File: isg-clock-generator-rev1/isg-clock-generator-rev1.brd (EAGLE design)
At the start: 76.2 x 76.2 mm, 154 parts, among them IC1 LMK03318RHSR, IC4 TPS7A8001DRBR, IC5 TPS7A8001DRBR, Q1 7M50072001, X1 OUT0_P, X2 OUT0_N, X3 OUT2_P, X4 PRIREF_P, X5 PRIREF_N, X6 V_INPUT

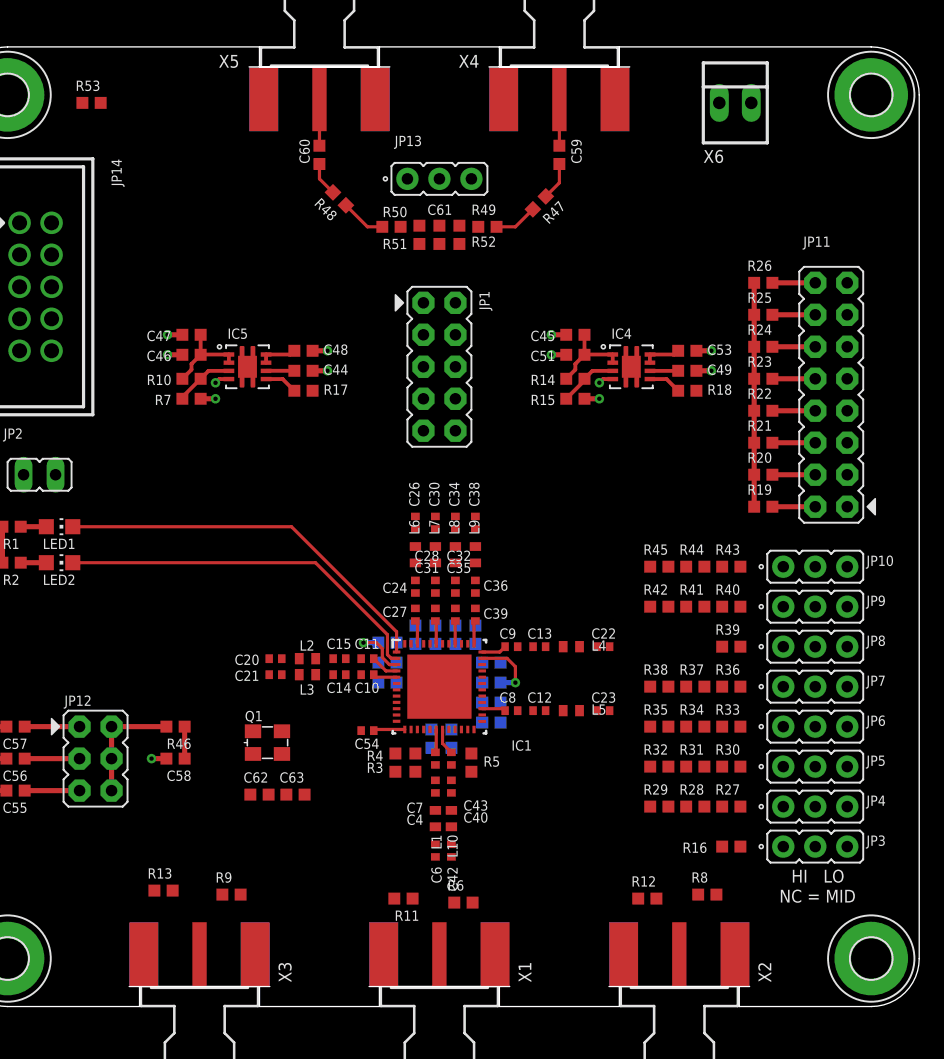
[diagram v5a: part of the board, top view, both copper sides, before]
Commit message: First-pass routing of high speed output signals
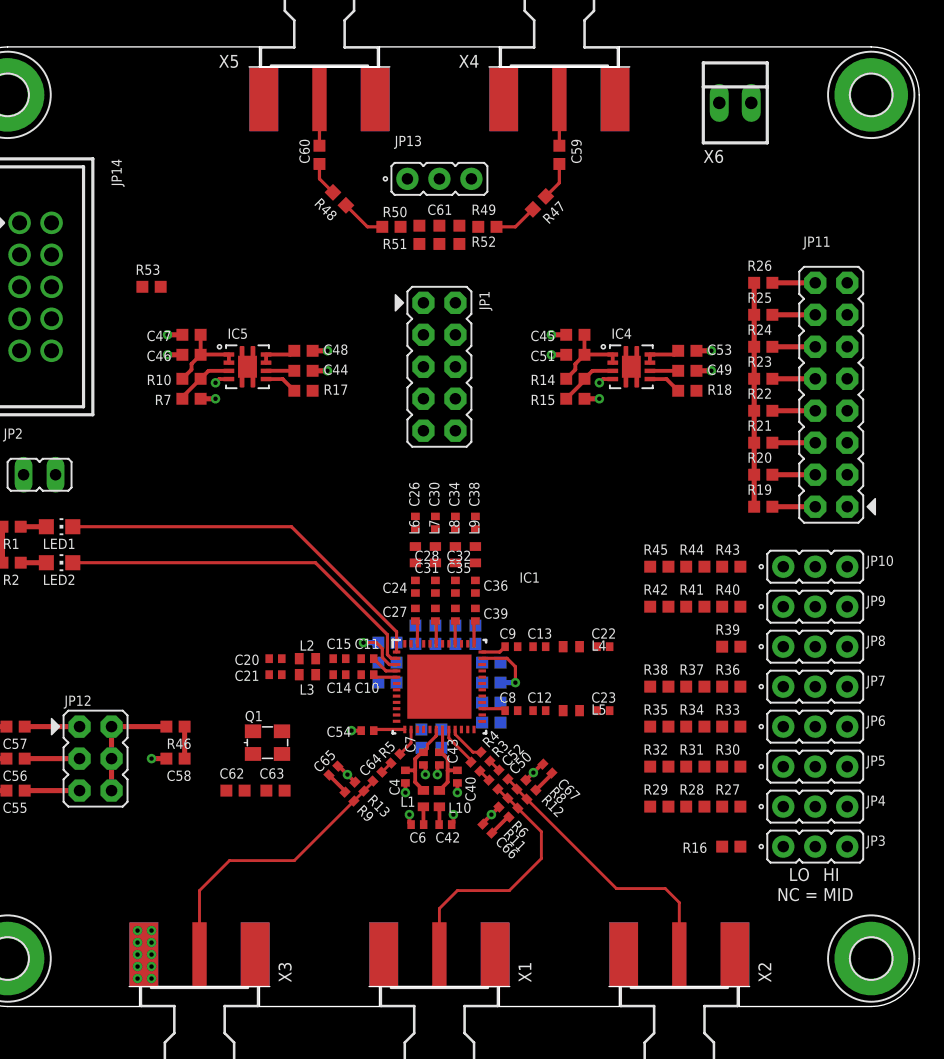
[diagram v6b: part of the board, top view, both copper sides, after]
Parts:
- added C50, C52, C64: 0R JUMPER, rcl-modified-footprints:C0402
- added C65, C66, C67: CAP CER 0.1uF X7R 0402, rcl-modified-footprints:C0402
- R11, R12, R13, R3, R4, R5, R6, R8, R9: device rcl-modified-footprints:R0603 -> rcl-modified-footprints:R0402
- X1: value OUT0_P -> OUT2_P
- X2: value OUT0_N -> OUT2_N
- X3: value OUT2_P -> OUT0_P
- X6: value V_INPUT -> V_IN_EXT
- moved R13 17.6 mm to (31.8, 17.5), turned to 315 degrees
- moved R8 16.1 mm to (45.4, 16.8), turned to 45 degrees
- moved R53 15.4 mm to (15.2, 57.1)
- moved R12 13.5 mm to (44.6, 17.6), turned to 225 degrees
- moved R9 12.2 mm to (31.0, 16.7), turned to 135 degrees
- moved R11 11.0 mm to (43.2, 16.2), turned to 45 degrees
- moved R6 8.17 mm to (44.0, 15.4), turned to 225 degrees
- moved R3 6.36 mm to (41.0, 19.1), turned to 135 degrees
- moved R5 6.04 mm to (34.6, 19.7), turned to 45 degrees
- moved R4 5.58 mm to (41.8, 19.8), turned to 135 degrees
- moved C4 2.51 mm to (35.4, 18.3)
- moved C6 2.51 mm to (36.4, 14.4), turned to 180 degrees
- moved C42 2.12 mm to (38.6, 14.4), turned to 0 degrees
- moved C62 1.93 mm to (21.9, 17.1)
- moved L1 1.85 mm to (36.8, 16.5)
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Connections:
- removed net N$1: R6.2, R8.2, R9.2
- removed net NC_OUT2_N: IC1.21
- removed net OUT0_N: IC1.15, R4.2
- removed net OUT0_R_N: R12.2, R4.1, R8.1, X2.1
- new net NC_OUT0_N: IC1.15
- new net OUT0_R_C_P: C64.2, R13.2, R9.1, X3.1
- new net OUT2_N: IC1.21, R4.2
- new net OUT2_R_C_N: C52.2, R12.2, R8.1, X2.1
- new net OUT2_R_C_P: C50.2, R11.2, R6.1, X1.1
- new net OUT2_R_N: C52.1, R4.1
- net GND: now also C65.2, C66.2, C67.2
- net OUT0_P: now also R5.2; no longer R3.2
- net OUT0_R_P: now also C64.1, R5.1; no longer R11.2, R3.1, R6.1, X1.1
- net OUT2_P: now also R3.2; no longer R5.2
- net OUT2_R_P: now also C50.1, R3.1; no longer R13.2, R5.1, R9.1, X3.1
- net PP_P1V8_VDDO: now also C65.1, C66.1, C67.1, R6.2, R8.2, R9.2
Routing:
- net OUT0_R_C_P: track 0.00 -> 22.5 mm
- net OUT2_R_C_N: track 0.00 -> 21.8 mm
- net OUT2_R_C_P: track 0.00 -> 20.4 mm
- net GND: track 18.9 -> 30.7 mm, vias 16 -> 36
- net PP_P1V8_VDDO: track 7.00 -> 15.5 mm
- net VDDO_01: track 1.84 -> 6.86 mm
- net VDDO_23: track 2.11 -> 6.35 mm
- net OUT2_P: track 0.00 -> 3.32 mm
- net OUT2_N: track 0.00 -> 3.02 mm
- net OUT0_P: track 0.00 -> 2.33 mm
- net OUT2_R_N: track 0.00 -> 1.02 mm
- net OUT2_R_P: track 0.00 -> 1.02 mm
- net OUT0_R_P: track 0.00 -> 1.02 mm

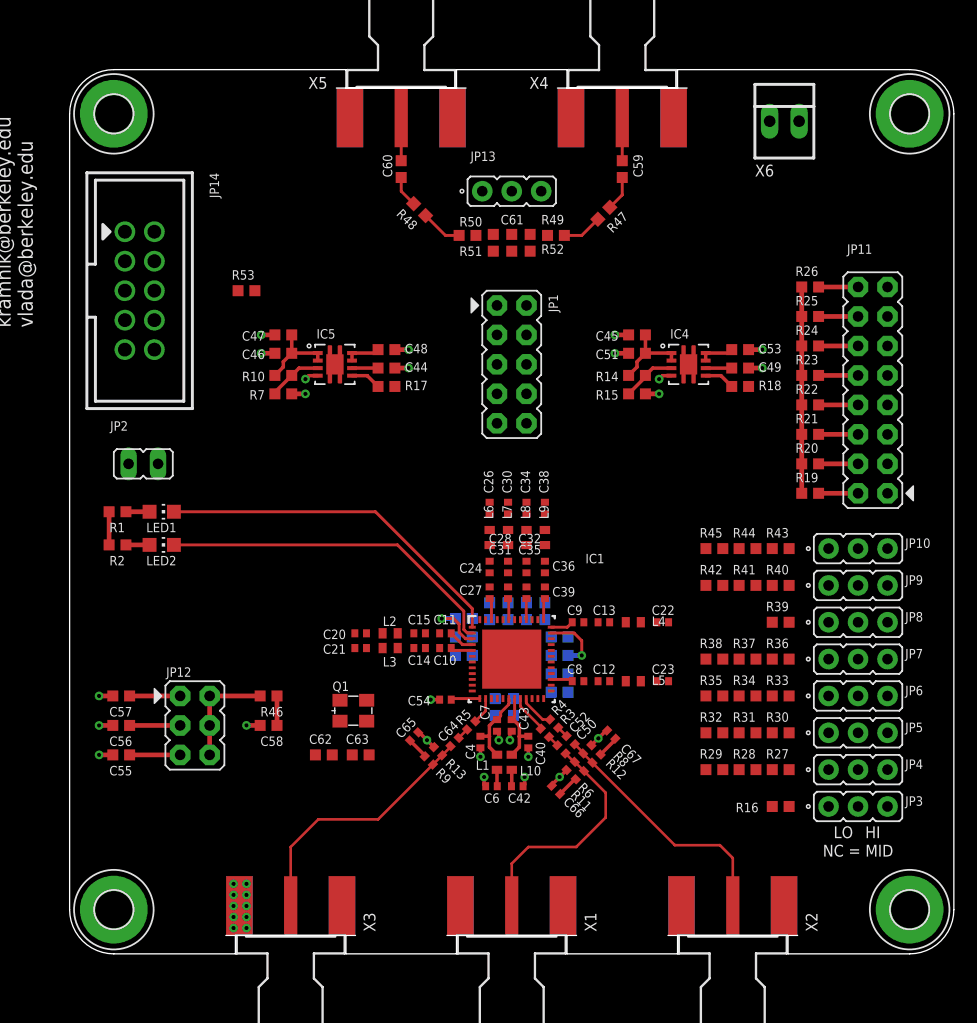
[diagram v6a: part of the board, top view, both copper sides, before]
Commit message: More decap routing
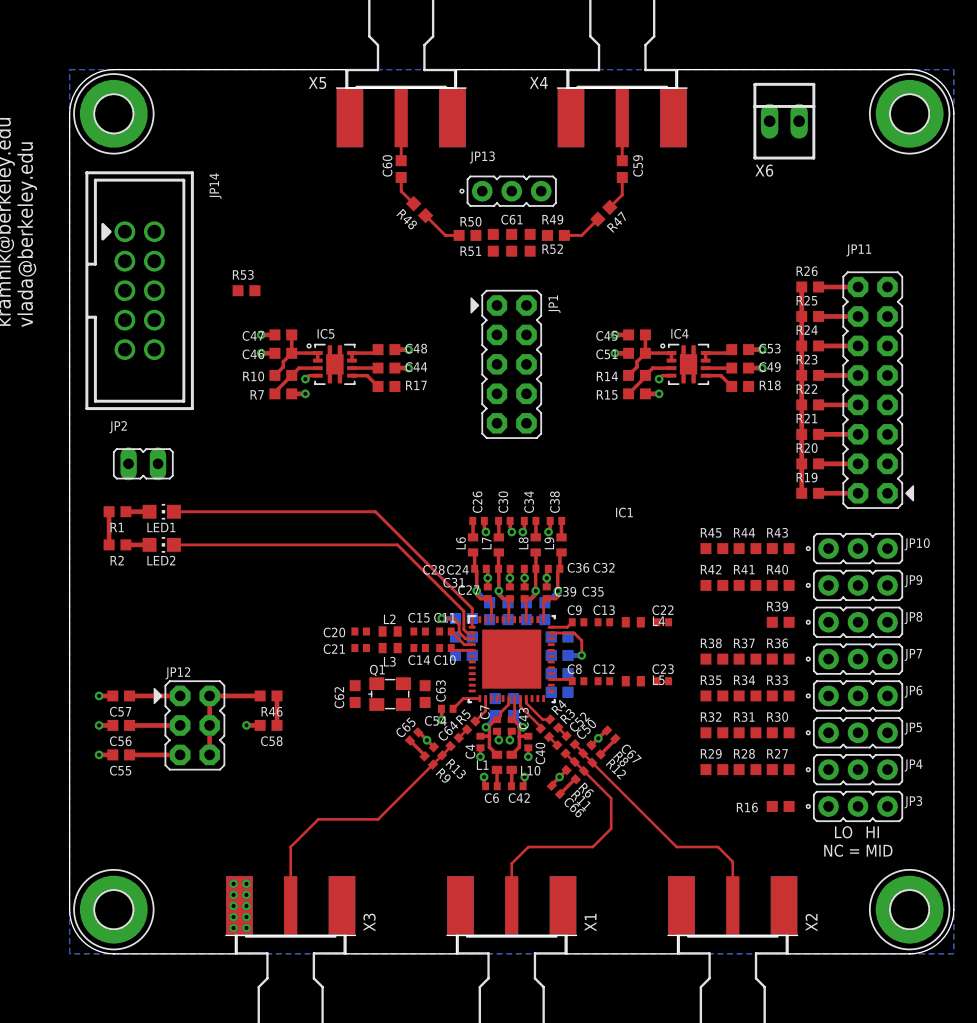
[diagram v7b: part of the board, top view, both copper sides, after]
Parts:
- moved C63 7.64 mm to (30.6, 22.4), turned to 270 degrees
- moved C62 5.89 mm to (24.6, 22.4), turned to 90 degrees
- moved Q1 3.48 mm to (27.6, 22.4)
- moved L6 1.56 mm to (34.8, 35.2)
- moved L9 1.56 mm to (42.4, 35.2)
- moved C26 1.46 mm to (35.2, 37.3), turned to 0 degrees
- moved C38 1.46 mm to (41.9, 37.3), turned to 180 degrees
- moved C34 1.16 mm to (39.7, 37.3), turned to 180 degrees
- moved C30 1.16 mm to (37.5, 37.3), turned to 0 degrees
- moved L8 1.02 mm to (40.2, 35.2)
- moved L7 1.02 mm to (37.0, 35.2)
- moved C24 0.81 mm to (35.4, 33.2), turned to 0 degrees
- moved C54 0.81 mm to (32.5, 21.1)
- moved C36 0.81 mm to (41.8, 33.2), turned to 180 degrees
- moved C32 0.35 mm to (39.7, 33.2), turned to 180 degrees
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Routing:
- net GND: track 30.7 -> 41.3 mm, vias 36 -> 44
- net VDDO_4: track 1.86 -> 8.41 mm, vias 0 -> 1
- net VDDO_7: track 1.88 -> 8.34 mm, vias 0 -> 1
- net VDDO_5: track 1.82 -> 7.97 mm, vias 0 -> 1
- net VDDO_6: track 1.84 -> 7.95 mm, vias 0 -> 1
- net PP_P1V8_VDDO: track 15.5 -> 21.2 mm
- net VDDO_23: track 6.35 -> 8.00 mm, vias 0 -> 1
- net VDDO_01: track 6.86 -> 8.51 mm, vias 0 -> 1
- net OUT2_R_C_P: track 20.4 -> 21.6 mm
- added copper zone on layer 16, net GND
